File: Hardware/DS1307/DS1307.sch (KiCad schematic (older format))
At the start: 11 parts, among them P1 I2C, U1 DS1307, X1 32.768kHz

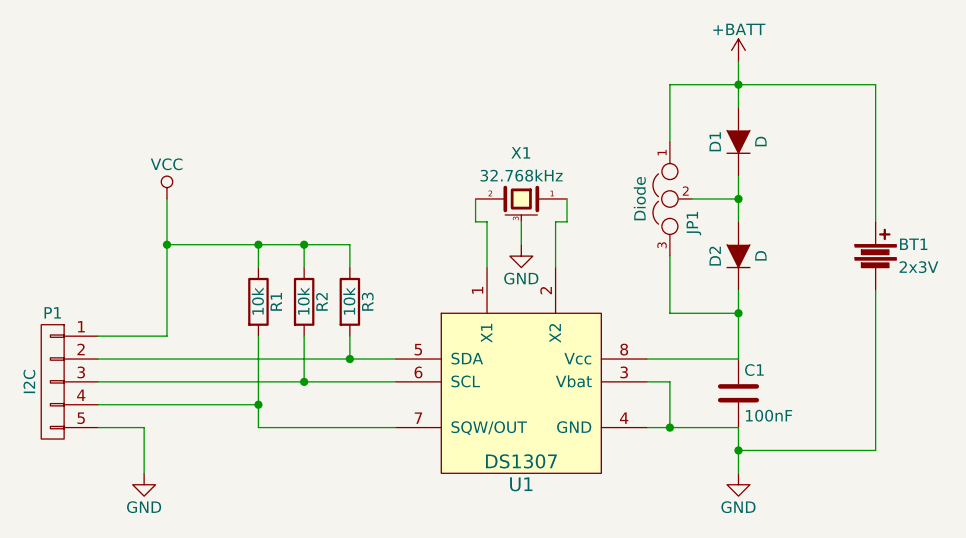
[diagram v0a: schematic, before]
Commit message: finished DS1307 and renamed it
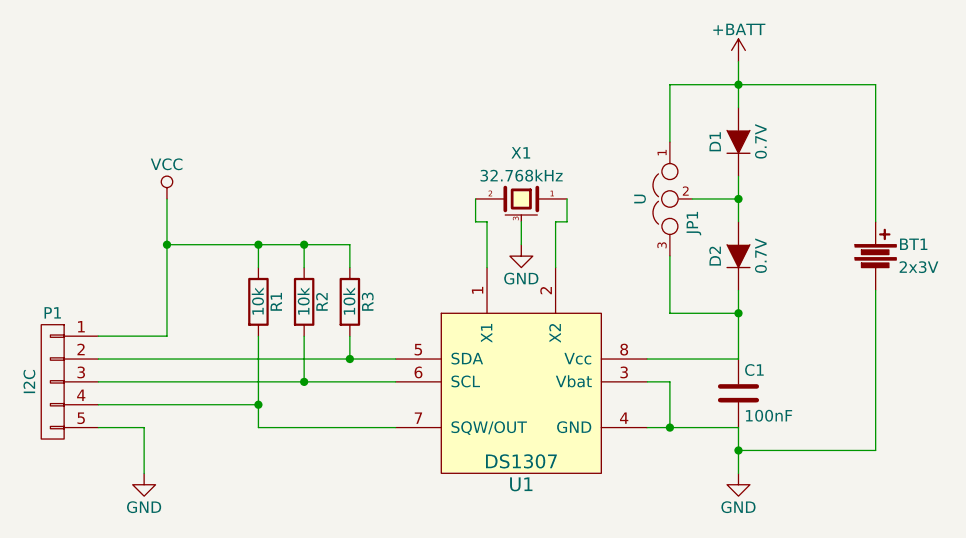
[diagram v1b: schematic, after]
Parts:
- D1, D2: value D -> 0.7V; footprint Diodes_ThroughHole:Diode_DO-35_SOD27_Horizontal_RM7.5 -> Resistors_SMD:R_1206_HandSoldering
- JP1: value Diode -> U; footprint Pin_Headers:Pin_Header_Straight_1x03 -> Footprints:SJ_2
- P1: footprint Pin_Headers:Pin_Header_Straight_1x05 -> SMD:SMD_05-4mm
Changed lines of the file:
@@
 LIBS:contrib
 LIBS:valves
+LIBS:ds1307
 LIBS:DS1307_3V3-cache
 EELAYER 25 0
@@
 P 6100 2150
 F 0 "D1" H 6100 2250 50  0000 C CNN
-F 1 "D" H 6100 2050 50  0000 C CNN
-F 2 "Diodes_ThroughHole:Diode_DO-35_SOD27_Horizontal_RM7.5" H 6100 2150 60  0001 C CNN
+F 1 "0.7V" H 6100 2050 50  0000 C CNN
+F 2 "Resistors_SMD:R_1206_HandSoldering" H 6100 2150 60  0001 C CNN
 F 3 "" H 6100 2150 60  0000 C CNN
 	1    6100 2150
@@
 F 0 "P1" H 3100 3500 50  0000 C CNN
 F 1 "I2C" V 3200 3200 50  0000 C CNN
-F 2 "Pin_Headers:Pin_Header_Straight_1x05" H 3100 3200 60  0001 C CNN
+F 2 "SMD:SMD_05-4mm" H 3100 3200 60  0001 C CNN
 F 3 "" H 3100 3200 60  0000 C CNN
 	1    3100 3200
@@
 P 6100 2650
 F 0 "D2" H 6100 2750 50  0000 C CNN
-F 1 "D" H 6100 2550 50  0000 C CNN
-F 2 "Diodes_ThroughHole:Diode_DO-35_SOD27_Horizontal_RM7.5" H 6100 2650 60  0001 C CNN
+F 1 "0.7V" H 6100 2550 50  0000 C CNN
+F 2 "Resistors_SMD:R_1206_HandSoldering" H 6100 2650 60  0001 C CNN
 F 3 "" H 6100 2650 60  0000 C CNN
 	1    6100 2650
@@
 P 5800 2400
 F 0 "JP1" H 5850 2300 50  0000 L CNN
-F 1 "Diode" H 5800 2500 50  0000 C BNN
-F 2 "Pin_Headers:Pin_Header_Straight_1x03" H 5800 2400 50  0001 C CNN
+F 1 "U" H 5800 2500 50  0000 C BNN
+F 2 "Footprints:SJ_2" H 5800 2400 50  0001 C CNN
 F 3 "" H 5800 2400 50  0000 C CNN
 	1    5800 2400
